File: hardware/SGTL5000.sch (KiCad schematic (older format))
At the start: 16 parts, among them J2 AudioJack3_Ground, U6 AP7313-1.8V, U7 SGTL5000

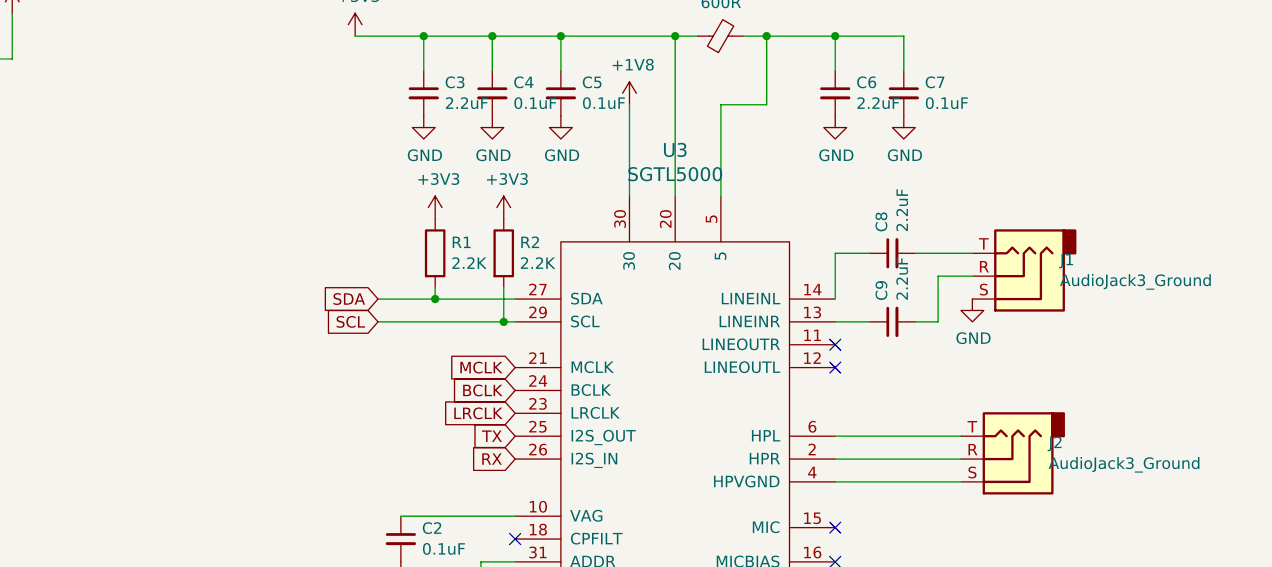
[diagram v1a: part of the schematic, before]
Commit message: switch to pwm led driver, first pass routing
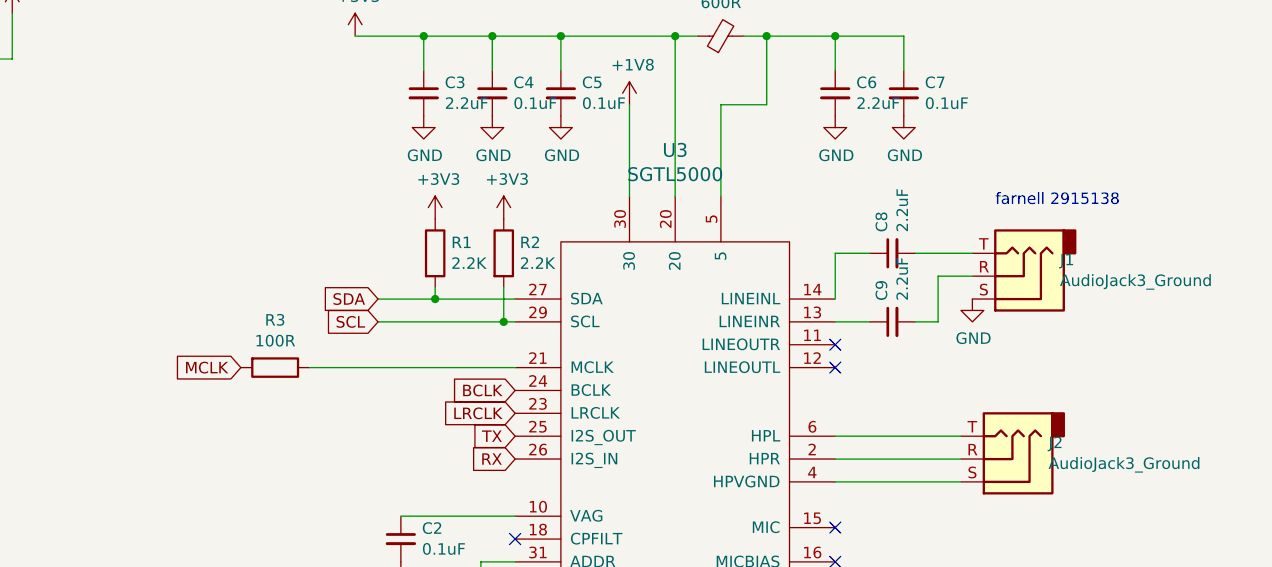
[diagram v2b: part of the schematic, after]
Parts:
- added R3: 100R, Resistor_SMD:R_0805_2012Metric, symbol Device:R
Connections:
- net MCLK: now also R3.2; no longer U7.21 (MCLK)
- new net: R3.1, U7.21 (MCLK)
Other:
- note added: "farnell 2915138"
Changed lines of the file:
@@
 F 1 "AudioJack3_Ground" H 6967 3070 50  0000 R CNN
 F 2 "Connector_Audio:Jack_3.5mm_CUI_SJ-3523-SMT_Horizontal" H 7150 3050 50  0001 C CNN
-F 3 "~" H 7150 3050 50  0001 C CNN
+F 3 "https://uk.farnell.com/switchcraft-conxall/35rasmt2bhntrx/connector-smt-3-5mm-ph-jk-tap/dp/2915138" H 7150 3050 50  0001 C CNN
 	1    7150 3050
 	-1   0    0    1
@@
 Text GLabel 4350 3250 0    50   Input ~ 0
 SCL
-Text GLabel 4950 3450 0    50   Input ~ 0
+Text GLabel 3750 3450 0    50   Input ~ 0
 MCLK
 Text GLabel 4950 3550 0    50   Input ~ 0
@@
 Wire Wire Line
 	6350 2950 6500 2950
+Text Notes 7050 2750 0    50   ~ 0
+farnell 2915138
+$Comp
+L Device:R R?
+U 1 1 5E21D79E
+P 3900 3450
+AR Path="/5E21D79E" Ref="R?"  Part="1"
+AR Path="/5E0E3867/5E21D79E" Ref="R3"  Part="1"
+F 0 "R3" V 3693 3450 50  0000 C CNN
+F 1 "100R" V 3784 3450 50  0000 C CNN
+F 2 "Resistor_SMD:R_0805_2012Metric" V 3830 3450 50  0001 C CNN
+F 3 "~" H 3900 3450 50  0001 C CNN
+	1    3900 3450
+	0    1    1    0
+$EndComp
+Wire Wire Line
+	4050 3450 4950 3450
 $EndSCHEMATC

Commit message: tidy schematic and finish layout
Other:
- note added: "SGTL5000 audio driver"
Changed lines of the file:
@@
 Wire Wire Line
 	4050 3450 4950 3450
+Text Notes 4700 1350 0    118  Italic 24
+SGTL5000 audio driver
 $EndSCHEMATC

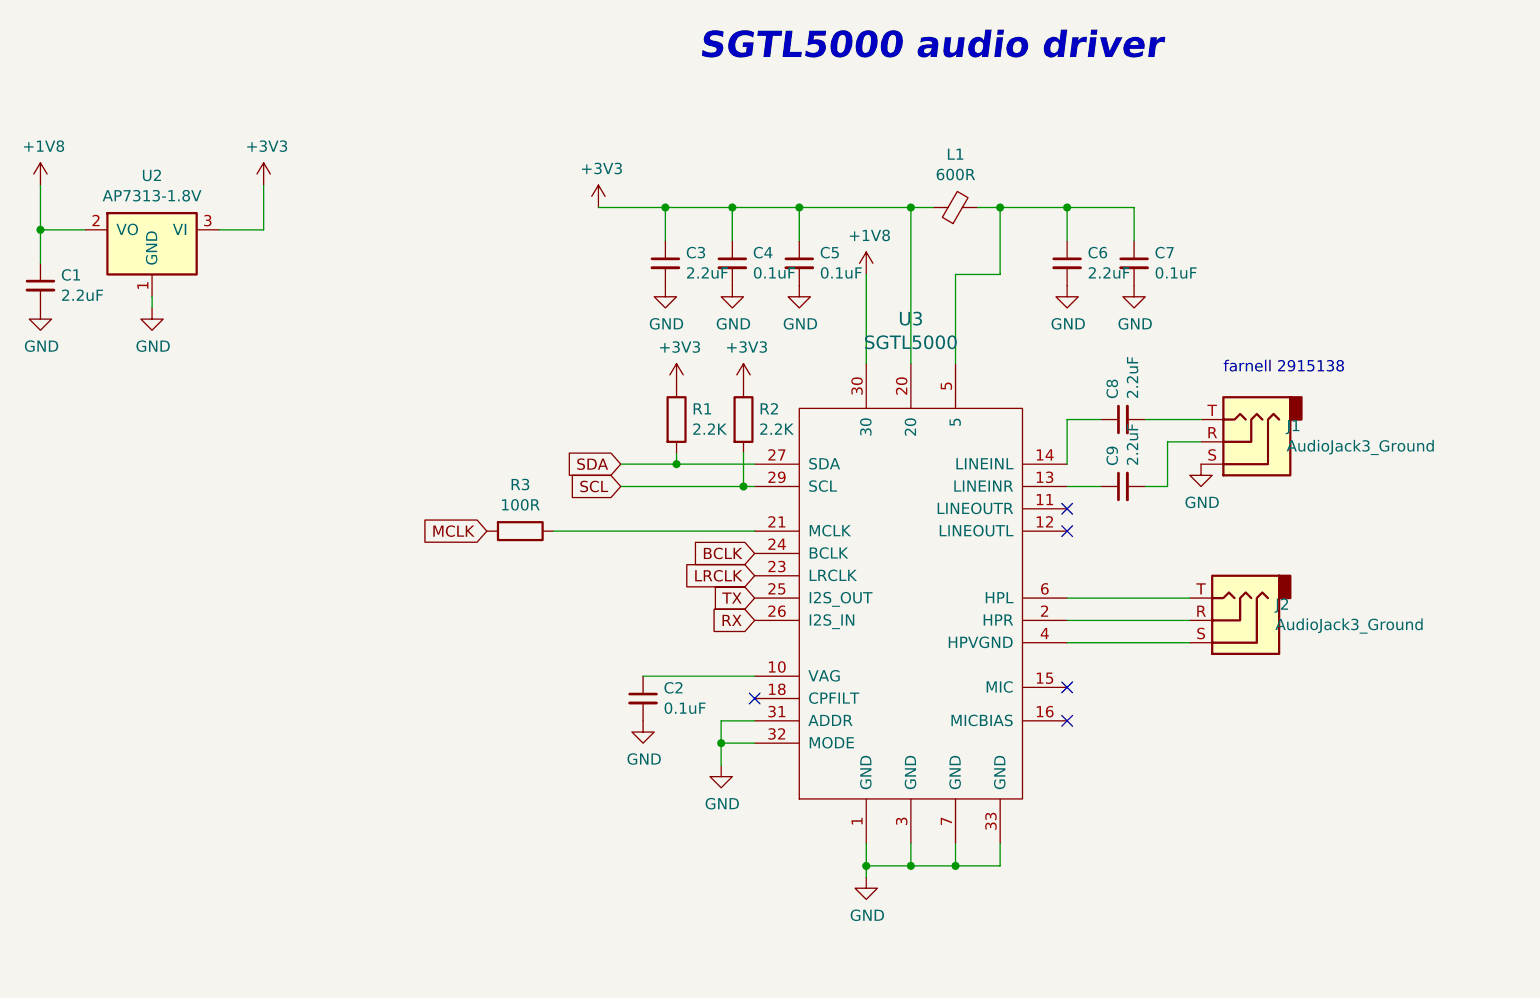
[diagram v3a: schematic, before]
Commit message: fix sgtl5000 symbol error, add filter resistor and cap for unused mic input
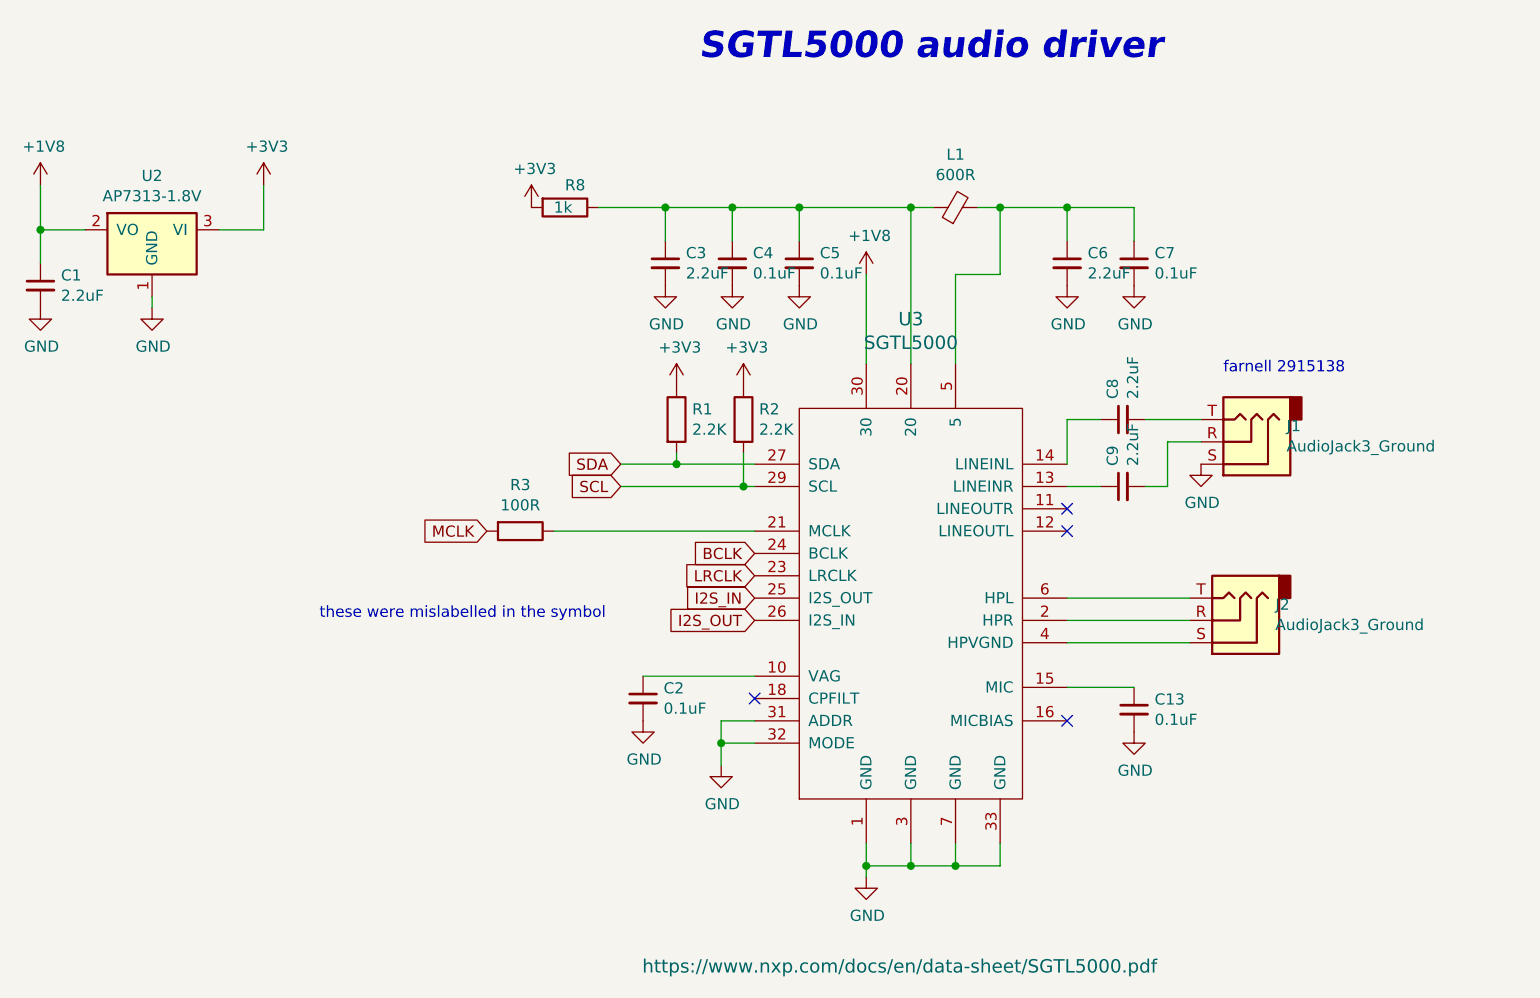
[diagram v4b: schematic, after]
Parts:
- added C13: 0.1uF, Capacitor_SMD:C_0805_2012Metric, symbol Device:C_Small
- added R8: 1k, Resistor_SMD:R_0805_2012Metric, symbol Device:R
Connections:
- net +3V3: now also R8.2; no longer C26.1, C27.1, C28.1, L2.1, U7.20
- net GND: now also C13.2
- net at U7.15 (MIC): now also C13.1
- net RX renamed I2S_OUT
- net TX renamed I2S_IN
- new net: C26.1, C27.1, C28.1, L2.1, R8.1, U7.20
- no-connect marks 5 -> 4
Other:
- note added: "these were mislabelled in the symbol\n"
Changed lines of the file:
@@
 L power:+3V3 #PWR?
 U 1 1 5BAC3E68
-P 4250 2000
+P 3950 2000
 AR Path="/5BAC3E68" Ref="#PWR?"  Part="1"
 AR Path="/5BAC34FB/5BAC3E68" Ref="#PWR0125"  Part="1"
 AR Path="/5E0E3867/5BAC3E68" Ref="#PWR0107"  Part="1"
-F 0 "#PWR0107" H 4250 1850 50  0001 C CNN
-F 1 "+3V3" H 4265 2173 50  0000 C CNN
-F 2 "" H 4250 2000 50  0001 C CNN
-F 3 "" H 4250 2000 50  0001 C CNN
-	1    4250 2000
+F 0 "#PWR0107" H 3950 1850 50  0001 C CNN
+F 1 "+3V3" H 3965 2173 50  0000 C CNN
+F 2 "" H 3950 2000 50  0001 C CNN
+F 3 "" H 3950 2000 50  0001 C CNN
+	1    3950 2000
 	1    0    0    -1
 $EndComp
@@
 LRCLK
 Text GLabel 4950 3750 0    50   Input ~ 0
-TX
+I2S_IN
 Text GLabel 4950 3850 0    50   Input ~ 0
-RX
+I2S_OUT
 Wire Wire Line
 	6800 3250 6800 3050
@@
 $EndComp
 NoConn ~ 4950 4200
-NoConn ~ 6350 4150
 NoConn ~ 6350 4300
 NoConn ~ 6350 3350
@@
 F 1 "SGTL5000" H 5650 4894 60  0000 C CNN
 F 2 "Package_DFN_QFN:QFN-32-1EP_5x5mm_P0.5mm_EP3.6x3.6mm" H 5650 3800 60  0001 C CNN
-F 3 "" H 5650 3800 60  0000 C CNN
+F 3 "https://www.nxp.com/docs/en/data-sheet/SGTL5000.pdf" H 5600 2100 60  0000 C CNN
 	1    5650 3750
 	1    0    0    -1
@@
 Text Notes 4700 1350 0    118  Italic 24
 SGTL5000 audio driver
+Text Notes 3000 3850 0    50   ~ 0
+these were mislabelled in the symbol\n
+$Comp
+L Device:C_Small C?
+U 1 1 5E112693
+P 6650 4250
+AR Path="/5E112693" Ref="C?"  Part="1"
+AR Path="/5BAC34FB/5E112693" Ref="C?"  Part="1"
+AR Path="/5E0E3867/5E112693" Ref="C13"  Part="1"
+F 0 "C13" H 6742 4296 50  0000 L CNN
+F 1 "0.1uF" H 6742 4205 50  0000 L CNN
+F 2 "Capacitor_SMD:C_0805_2012Metric" H 6650 4250 50  0001 C CNN
+F 3 "~" H 6650 4250 50  0001 C CNN
+	1    6650 4250
+	1    0    0    -1
+$EndComp
+Wire Wire Line
+	6350 4150 6650 4150
+$Comp
+L power:GND #PWR?
+U 1 1 5E113ED8
+P 6650 4350
+AR Path="/5E113ED8" Ref="#PWR?"  Part="1"
+AR Path="/5BAC34FB/5E113ED8" Ref="#PWR?"  Part="1"
+AR Path="/5E0E3867/5E113ED8" Ref="#PWR01"  Part="1"
+F 0 "#PWR01" H 6650 4100 50  0001 C CNN
+F 1 "GND" H 6655 4177 50  0000 C CNN
+F 2 "" H 6650 4350 50  0001 C CNN
+F 3 "" H 6650 4350 50  0001 C CNN
+	1    6650 4350
+	1    0    0    -1
+$EndComp
+$Comp
+L Device:R R?
+U 1 1 5E11741C
+P 4100 2000
+AR Path="/5E11741C" Ref="R?"  Part="1"
+AR Path="/5BAC34FB/5E11741C" Ref="R?"  Part="1"
+AR Path="/5E0E3867/5E11741C" Ref="R8"  Part="1"
+F 0 "R8" V 4000 2000 50  0000 L CNN
+F 1 "1k" V 4100 1950 50  0000 L CNN
+F 2 "Resistor_SMD:R_0805_2012Metric" V 4030 2000 50  0001 C CNN
+F 3 "~" H 4100 2000 50  0001 C CNN
+	1    4100 2000
+	0    1    1    0
+$EndComp
 $EndSCHEMATC
